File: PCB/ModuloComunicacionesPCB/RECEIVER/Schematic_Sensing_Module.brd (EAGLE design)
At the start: 7.6 x 1.2 mm, 26 parts, among them J1 USB3090-XX-X_REVE, Q1 MMBT2222A, Q2 MMBT2222A, U1 AMS1117-5.0, U2 AMS1117-5.0

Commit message: screen ino verified screen and placing in receiving corrected
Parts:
- moved REL2 120.0 mm to (101.4, 81.7), turned to 180 degrees
- moved U$6 98.4 mm to (99.0, 67.2), turned to 270 degrees
- moved 1N4007SMA 93.6 mm to (102.9, 54.6), flipped to the top, turned to 180 degrees
- moved REL1 93.1 mm to (80.1, 81.4), turned to 180 degrees
- moved R1 91.9 mm to (103.6, 51.2), flipped to the top, turned to 0 degrees
- moved Q1 76.0 mm to (93.5, 53.6), flipped to the top, turned to 90 degrees
- moved C2 70.6 mm to (53.9, 76.3), flipped to the top, turned to 270 degrees
- moved C1 70.0 mm to (50.8, 76.4), flipped to the top, turned to 90 degrees
- moved U$9 69.2 mm to (56.3, 67.0)
- moved U$5 68.5 mm to (79.7, 66.9), turned to 270 degrees
- moved 1N4007 56.5 mm to (82.4, 54.4), flipped to the top, turned to 0 degrees
- moved R2 53.0 mm to (82.8, 49.2), flipped to the top, turned to 0 degrees
- moved C5 51.7 mm to (73.8, 37.0)
- moved JP1 49.8 mm to (102.7, 16.4), turned to 270 degrees
- moved U$1 49.3 mm to (14.1, 70.1), turned to 90 degrees
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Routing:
- net VR1: track 58.0 -> 0.00 mm
- net VR2: track 57.6 -> 0.00 mm
- net VINCHAR: track 24.3 -> 0.00 mm
- net N$6: track 15.2 -> 0.00 mm
- net N$7: track 8.52 -> 0.00 mm
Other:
- board size 7.6 x 1.2 mm -> 1.2 x 7.6 mm

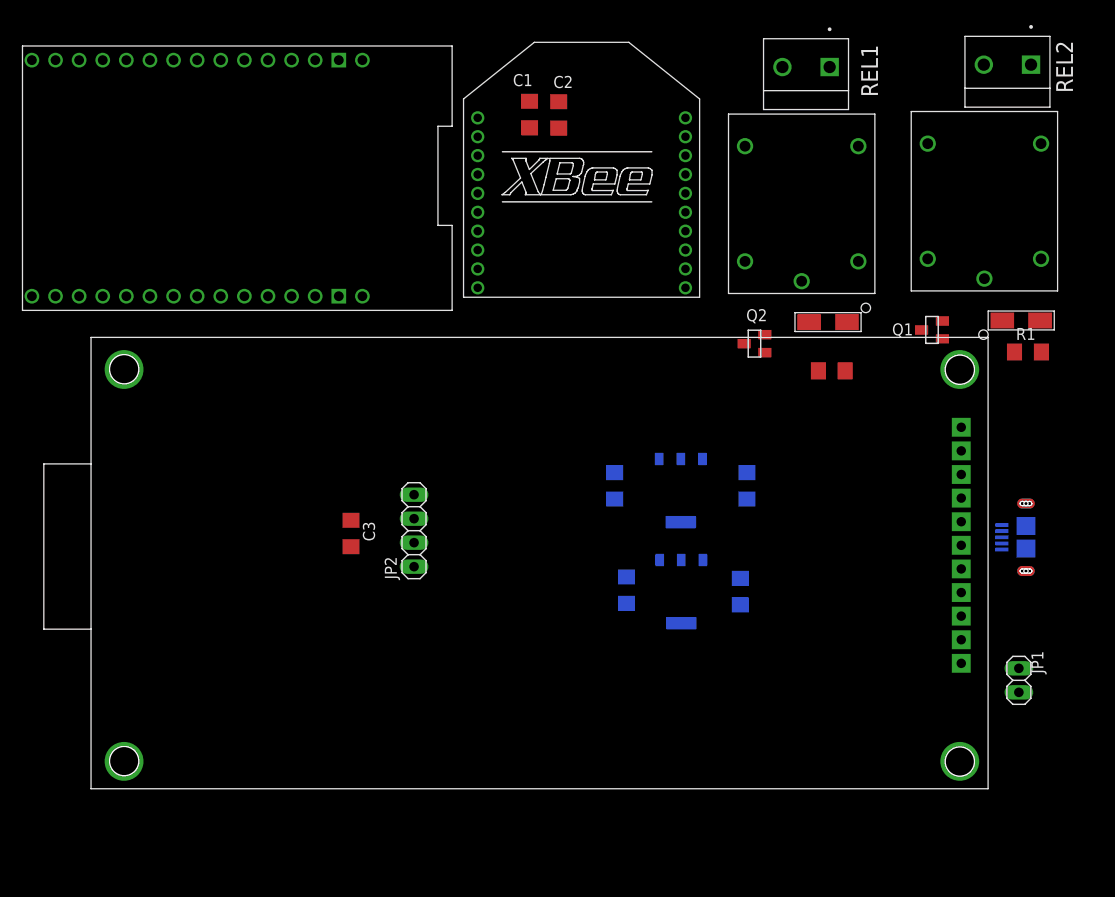
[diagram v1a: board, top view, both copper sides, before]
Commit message: pcb enviadas a produccion
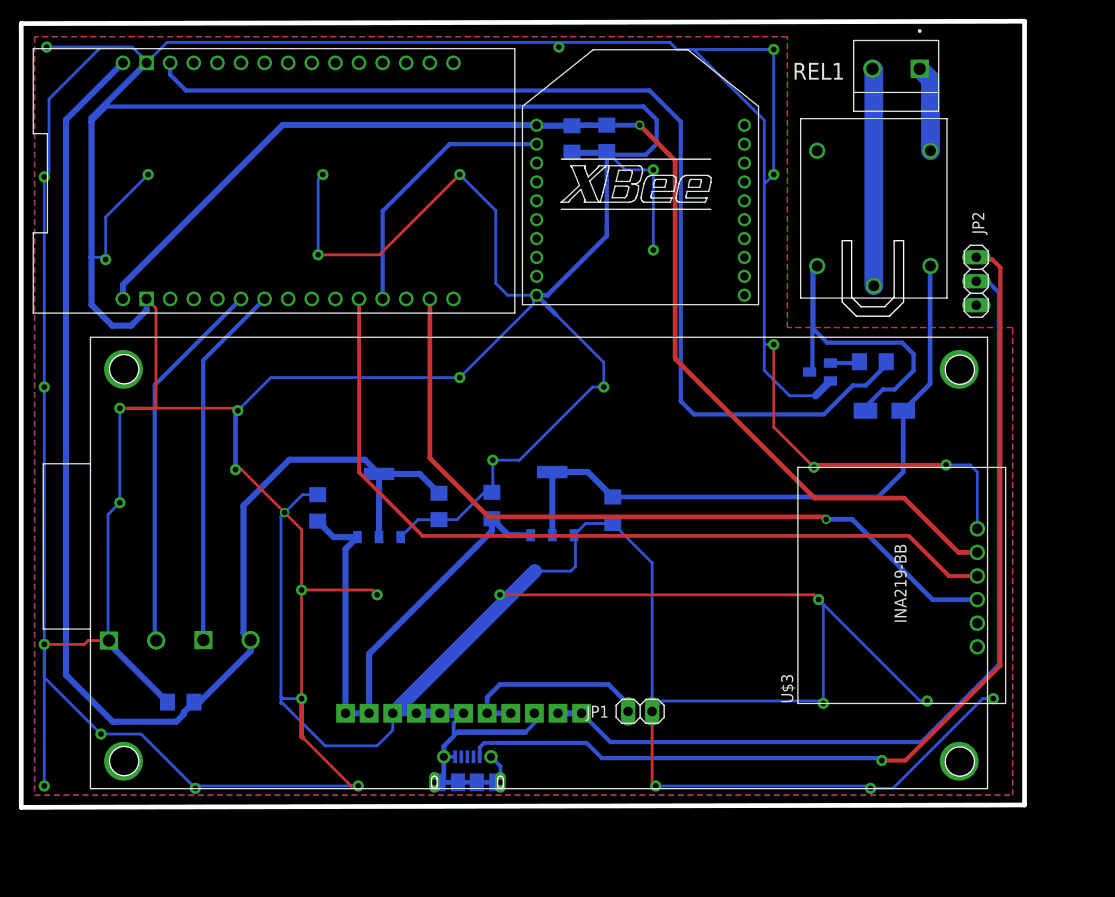
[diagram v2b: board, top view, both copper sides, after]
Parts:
- removed 1N4007SMA: 1N4007SMA, 1n400X:SMA
- removed J1: USB3090-XX-X_REVE, USB3090-XX-X_REVE:GCT_USB3090-XX-X_REVE
- removed Q1: MMBT2222A, MMBT2222A:SOT23
- removed R1: 10k, rcl:R1206
- removed REL2: TERMINAL-TB2, TERMINAL-TB001:TERMINAL-TB2
- removed U$6: SRD-3, RELE-SRD:SRD-N
- added CONN1, CONN2: TERMINAL-TB2, TERMINAL-TB001:TERMINAL-TB2
- added J2: 1050170001, 1050170001_MOLEX:MOLEX_1050170001
- added U$3: INABB, INA219BB:INA219-MODULE
- JP2: device pinhead:1X04 -> pinhead:1X03
- moved JP2 65.1 mm to (98.1, 58.7), turned to 270 degrees
- moved CARGADOR 46.4 mm to (43.8, 20.5), turned to 0 degrees
- moved JP1 40.2 mm to (62.5, 13.2), turned to 0 degrees
- moved C6 33.8 mm to (28.4, 34.7), turned to 90 degrees
- moved U2 33.3 mm to (34.9, 35.0), turned to 0 degrees
- moved C4 33.2 mm to (41.2, 34.9), turned to 270 degrees
- moved C3 25.4 mm to (13.9, 14.1), flipped to the bottom, turned to 0 degrees
- moved C5 14.4 mm to (59.6, 34.5), turned to 270 degrees
- moved U1 13.7 mm to (53.2, 35.2), turned to 0 degrees
- moved C7 13.2 mm to (46.8, 35.0), turned to 90 degrees
- moved U$1 12.7 mm to (26.8, 68.8), turned to 270 degrees
- moved 1N4007 11.1 mm to (88.4, 45.0), flipped to the bottom, turned to 180 degrees
- moved REL1 9.54 mm to (89.7, 81.2)
- moved C1 8.56 mm to (59.0, 73.8), flipped to the bottom, turned to 270 degrees
- moved U$5 7.66 mm to (87.3, 66.4)
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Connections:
- removed net CR2: REL2.2, U$6.C
- removed net N$6: 1N4007SMA.1, Q1.3, U$6.VL-
- removed net N$7: Q1.1, R1.2
- removed net NOR2: REL2.1, U$6.NO
- removed net VR2: R1.1, U$1.D12
- new net 32K: U$3.1
- new net SCL: U$1.D22, U$3.3
- new net SDA: U$1.D21, U$3.4
- new net SQW: U$3.2
- new net VON: CARGADOR.VIN, CARGADOR.VIN1, JP2.2
- net GND: now also CONN1.1, J2.5, J2.SH1, J2.SH2, J2.SH3, J2.SH4, J2.SH5, J2.SH6, J2.SH7, J2.SH8, U$3.6; no longer J1.5, J1.6, J1.7, J1.8, J1.9, JP2.1, Q1.2
- net RXNEX: now also CONN2.1; no longer JP2.3
- net TXNEX: now also CONN1.2; no longer JP2.2
- net VDEVICES: now also CONN2.2; no longer JP2.4
- net VINCHAR: now also J2.1, JP2.1; no longer CARGADOR.VIN, CARGADOR.VIN1, J1.1
- net VOUTRELAYS: no longer 1N4007SMA.2, U$6.VL+
- net VXBEE: now also U$3.5
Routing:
- net GND: track 0.00 -> 969.4 mm, vias 0 -> 39
- net VDEVICES: track 0.00 -> 138.7 mm
- net VXBEE: track 0.00 -> 130.1 mm, vias 0 -> 1
- net VR1: track 0.00 -> 111.8 mm
- net VINCHAR: track 0.00 -> 106.4 mm, vias 0 -> 1
- net VON: track 0.00 -> 93.7 mm
- net SDA: track 0.00 -> 88.4 mm
- net SCL: track 0.00 -> 81.0 mm, vias 0 -> 1
- net VOUTRELAYS: track 0.00 -> 69.1 mm
- net VOUTCH: track 0.00 -> 57.4 mm
- net TXNEX: track 0.00 -> 40.0 mm
- net N$8: track 0.00 -> 39.0 mm
- net RXNEX: track 0.00 -> 38.8 mm
- net DOUT: track 0.00 -> 28.5 mm
- net CR1: track 0.00 -> 23.0 mm
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- added copper zone on layer 1, net GND
- added copper zone on layer 16, net GND
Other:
- board size 1.2 x 7.6 mm -> 106.2 x 83.2 mm
- board text added: "GND"
- board text added: "RX"
- board text added: "TX"
- board text added: "VCC"
